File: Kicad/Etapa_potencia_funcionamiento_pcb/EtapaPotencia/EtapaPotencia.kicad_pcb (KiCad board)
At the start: 2 copper layers, 65 parts, among them IC1 IRF630, IC2 IRF630, J1 Conn_01x01_Male, Q1 BC547, Q2 BC557, Q3 BC557, U1 TL082, U2 TL082, U3 TL082, U4 LM393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

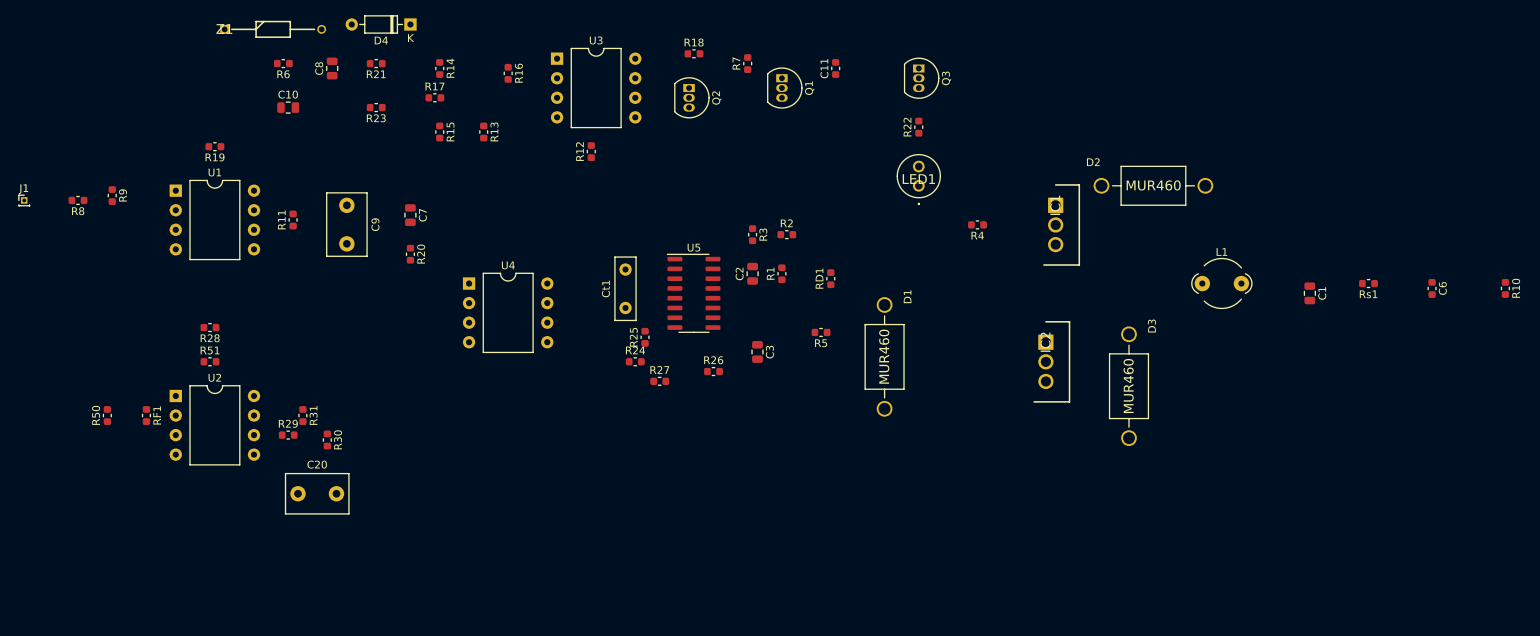
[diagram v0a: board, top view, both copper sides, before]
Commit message: Actualizacion PCB
Falta acomodar el GND y ver los Loops
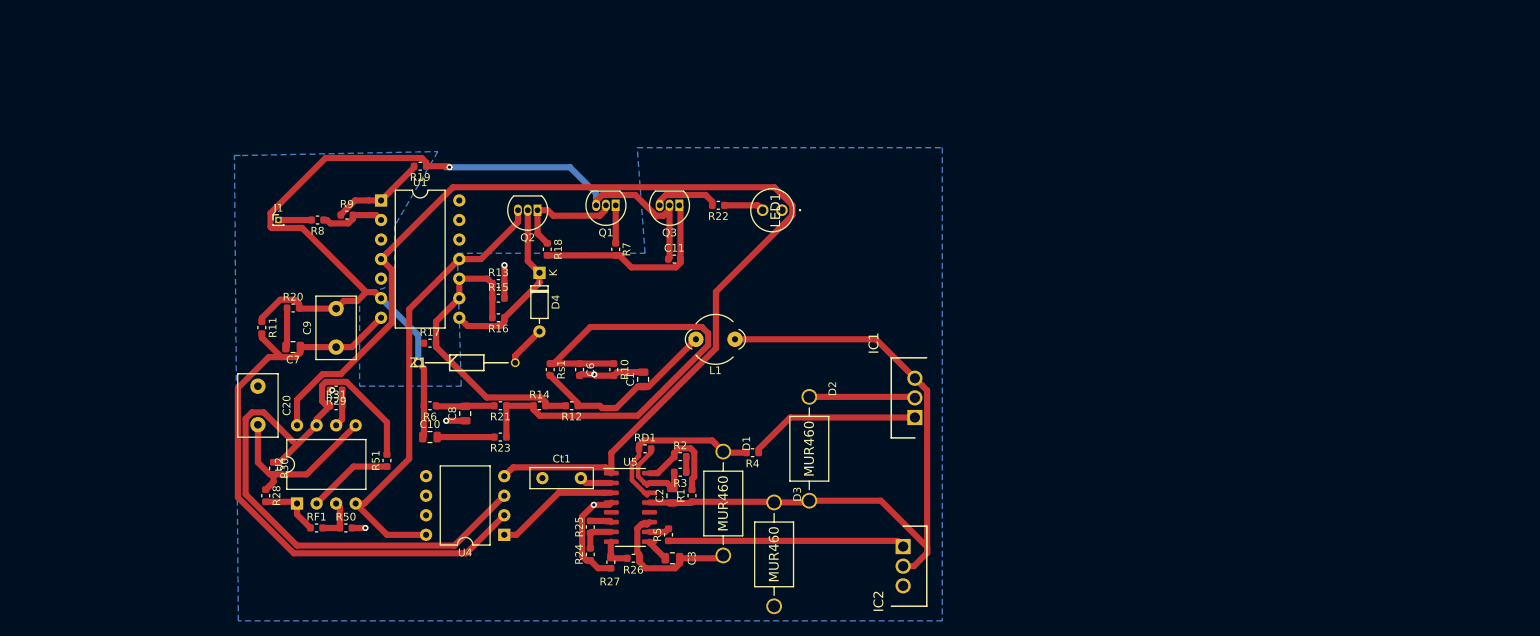
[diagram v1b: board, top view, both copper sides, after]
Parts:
- removed U3: TL082, Package_DIP:DIP-8_W10.16mm
- U1: value TL082 -> TL084; footprint Package_DIP:DIP-8_W10.16mm -> Package_DIP:DIP-14_W10.16mm
- moved R10 116.3 mm to (100.1, 58.8)
- moved C6 111.2 mm to (95.6, 58.8)
- moved Rs1 106.9 mm to (91.8, 58.8), turned to 270 degrees
- moved C1 87.3 mm to (103.9, 60.1), turned to 90 degrees
- moved L1 61.1 mm to (115.8, 54.9), turned to 180 degrees
- moved D2 56.3 mm to (125.5, 69.1), turned to 270 degrees
- moved D3 51.0 mm to (120.9, 82.8)
- moved Z1 50.1 mm to (74.7, 57.9)
- moved R6 48.4 mm to (76.2, 63.5)
- moved C8 48.0 mm to (80.8, 64.5)
- moved R21 47.3 mm to (85.3, 63.5)
- moved C10 46.6 mm to (76.2, 67.6)
- moved R23 45.7 mm to (85.3, 67.6)
- moved R14 45.7 mm to (90.4, 63.5), turned to 0 degrees
- moved R4 41.6 mm to (118.1, 69.6)
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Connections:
- U1 pad 4: -5V -> +12V
- U1 pad 8: +12V -> Net-(D4-Pad1)
- U4 pad 4: (no net) -> +12V
- U4 pad 8: (no net) -> -5V
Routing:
- net +12V: track 0.00 -> 146.2 mm
- net Net-(C10-Pad1): track 0.00 -> 125.8 mm, vias 0 -> 1
- net Net-(C2-Pad1): track 0.00 -> 92.2 mm
- net Net-(R30-Pad1): track 0.00 -> 86.1 mm
- net Net-(C7-Pad1): track 0.00 -> 80.8 mm
- net Net-(C6-Pad1): track 0.00 -> 67.3 mm
- net -5V: track 0.00 -> 60.0 mm
- net Net-(R12-Pad2): track 0.00 -> 39.4 mm
- net GND: track 0.00 -> 31.1 mm, vias 0 -> 6
- net Net-(IC2-Pad1): track 0.00 -> 30.8 mm
- net Net-(C11-Pad2): track 0.00 -> 25.7 mm
- net Net-(C1-Pad1): track 0.00 -> 24.8 mm
- net Net-(D4-Pad1): track 0.00 -> 23.5 mm
- net Net-(C20-Pad2): track 0.00 -> 23.3 mm
- net Net-(D1-Pad1): track 0.00 -> 23.0 mm
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- added copper zone on B.Cu, net GND
